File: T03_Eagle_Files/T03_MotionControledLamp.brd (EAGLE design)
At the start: 63.5 x 43.2 mm, 32 parts, among them U1 ATMEGA328P-MU, U4 TPS61161ADRVT, X2 16MHz

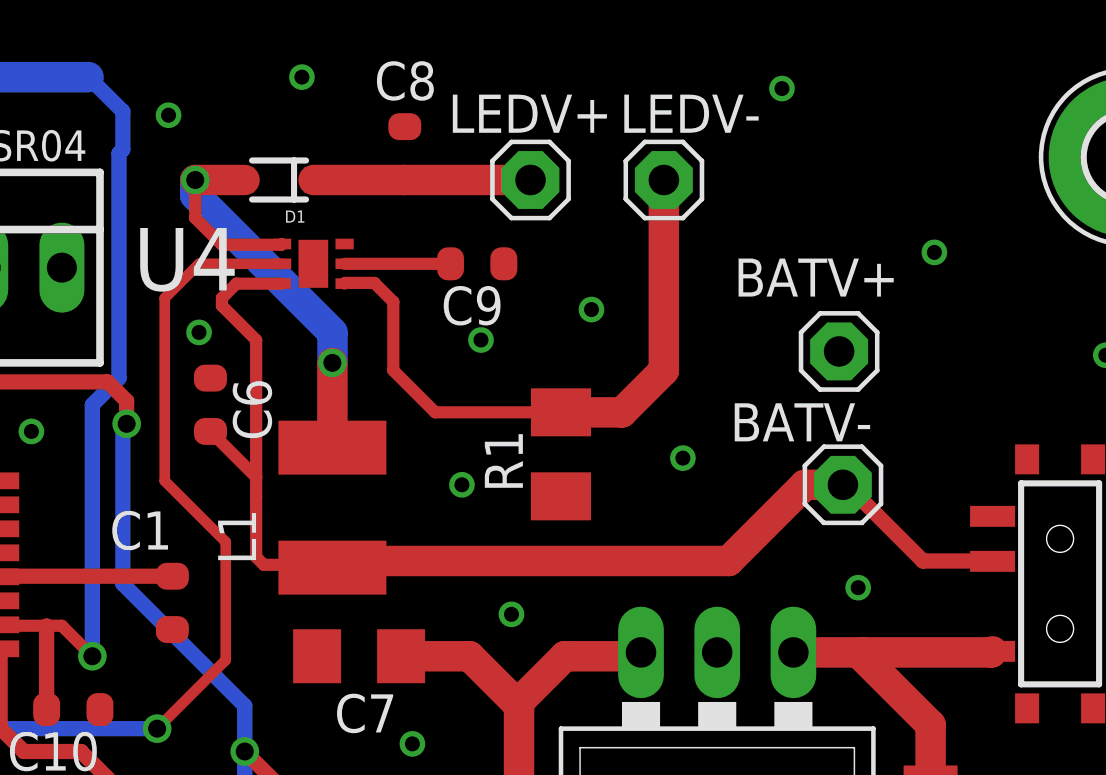
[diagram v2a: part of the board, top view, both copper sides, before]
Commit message: Updated values of components and symbols for Board Layout
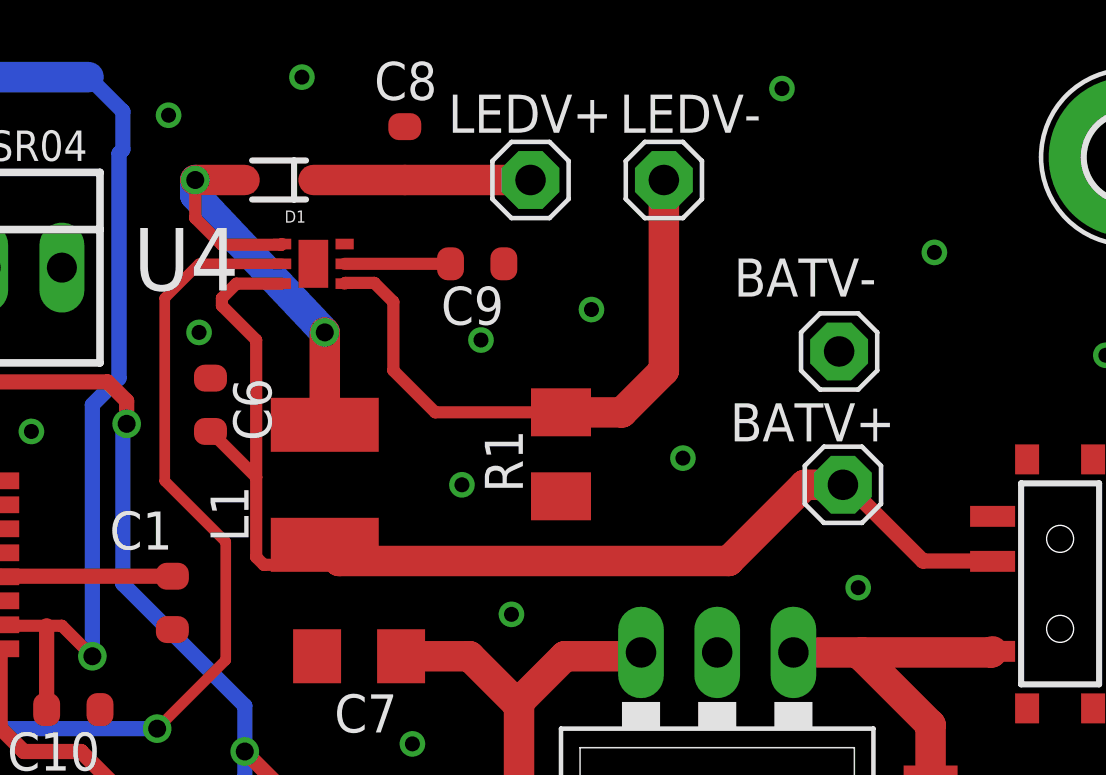
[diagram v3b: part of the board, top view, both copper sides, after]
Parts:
- BATV+: value BAT_GND -> BAT_POS_VOLT
- BATV-: value BAT_POS_VOLT -> BAT_GND
- C8: value 0.1uF -> 10uF
- moved BATV+ 4.45 mm to (48.9, 26.8)
- moved BATV- 4.45 mm to (48.8, 31.2)
- moved L1 0.80 mm to (31.6, 26.8)
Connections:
- net +V_BAT: now also BATV+.1; no longer BATV-.1
- net GND: now also BATV-.1; no longer BATV+.1
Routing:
- net SW: track 17.0 -> 16.1 mm
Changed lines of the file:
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@@
 <element name="C6" library="Smartprj" package="C0603-ROUND" value="1uF" x="27.813" y="29.464" rot="R270"/>
 <element name="C7" library="rcl" package="C1206" value="10uF" x="32.766" y="21.082" rot="R180"/>
-<element name="C8" library="Smartprj" package="C0603-ROUND" value="0.1uF" x="34.29" y="37.846" smashed="yes" rot="R270">
+<element name="C8" library="Smartprj" package="C0603-ROUND" value="10uF" x="34.29" y="37.846" smashed="yes" rot="R270">
 <attribute name="NAME" x="33.274" y="39.624" size="1.27" layer="25"/>
 <attribute name="VALUE" x="32.258" y="38.735" size="1.27" layer="27" rot="R270"/>
@@
 <element name="L7805" library="v-reg" package="78XXL" value="L7805" x="44.704" y="17.399" rot="R180"/>
 <element name="JP1" library="SparkFun-Connectors" package="2X5-SHROUDED_LOCK" value="AVR_SPI_PROG" x="16.51" y="12.446" rot="R90"/>
-<element name="BATV-" library="adafruit" package="1X01" value="BAT_POS_VOLT" x="48.895" y="26.797" smashed="yes">
+<element name="BATV+" library="adafruit" package="1X01" value="BAT_POS_VOLT" x="48.895" y="26.797" smashed="yes">
 <attribute name="NAME" x="45.1358" y="28.2448" size="1.27" layer="25" ratio="10"/>
 <attribute name="VALUE" x="47.625" y="23.622" size="1.27" layer="27"/>
 </element>
-<element name="BATV+" library="adafruit" package="1X01" value="BAT_GND" x="48.768" y="31.242" smashed="yes">
+<element name="BATV-" library="adafruit" package="1X01" value="BAT_GND" x="48.768" y="31.242" smashed="yes">
 <attribute name="NAME" x="45.2628" y="33.0708" size="1.27" layer="25" ratio="10"/>
 <attribute name="VALUE" x="48.514" y="33.274" size="1.27" layer="27"/>
 </element>
-<element name="L1" library="rcl" package="L4532P" value="22uH" x="31.877" y="26.035" smashed="yes" rot="R90">
-<attribute name="NAME" x="29.337" y="24.13" size="1.27" layer="25" rot="R90"/>
-<attribute name="VALUE" x="35.687" y="24.13" size="1.27" layer="27" rot="R90"/>
+<element name="L1" library="rcl" package="L4532P" value="22uH" x="31.623" y="26.797" smashed="yes" rot="R90">
+<attribute name="NAME" x="29.083" y="24.892" size="1.27" layer="25" rot="R90"/>
+<attribute name="VALUE" x="35.433" y="24.892" size="1.27" layer="27" rot="R90"/>
 </element>
 <element name="PWR_SWTCH" library="SparkFun-Electromechanical" package="KPS-1290" value="SWITCH_SPDT" x="56.134" y="23.495" rot="R90">
@@
 <contactref element="C7" pad="2"/>
 <contactref element="C5" pad="2"/>
-<contactref element="BATV+" pad="1"/>
+<contactref element="BATV-" pad="1"/>
 <contactref element="L7805" pad="GND"/>
 <contactref element="JP1" pad="6"/>
@@
 <contactref element="L1" pad="2"/>
 <contactref element="D1" pad="A"/>
-<wire x1="31.877" y1="28.035" x2="31.877" y2="30.861" width="1.016" layer="1"/>
-<via x="31.877" y="30.861" extent="1-16" drill="0.6"/>
+<wire x1="31.623" y1="28.797" x2="31.623" y2="31.877" width="1.016" layer="1"/>
+<via x="31.623" y="31.877" extent="1-16" drill="0.6"/>
 <via x="27.305" y="36.957" extent="1-16" drill="0.6"/>
 <wire x1="27.305" y1="36.957" x2="28.949" y2="36.957" width="1.016" layer="1"/>
-<wire x1="31.877" y1="30.861" x2="31.877" y2="31.877" width="1.016" layer="16"/>
-<wire x1="31.877" y1="31.877" x2="27.305" y2="36.449" width="1.016" layer="16"/>
+<wire x1="31.623" y1="31.877" x2="27.305" y2="36.449" width="1.016" layer="16"/>
 <wire x1="27.305" y1="36.449" x2="27.305" y2="36.957" width="1.016" layer="16"/>
 <wire x1="30.2006" y1="34.8234" x2="30.1752" y2="34.798" width="0.4064" layer="1"/>
@@
 <signal name="+V_BAT">
 <contactref element="PWR_SWTCH" pad="P"/>
-<contactref element="BATV-" pad="1"/>
+<contactref element="BATV+" pad="1"/>
 <contactref element="C6" pad="2"/>
 <contactref element="U4" pad="6"/>
 <contactref element="L1" pad="1"/>
-<wire x1="31.877" y1="24.035" x2="32.099" y2="24.257" width="1.016" layer="1"/>
+<wire x1="31.623" y1="24.797" x2="32.099" y2="24.257" width="1.016" layer="1"/>
 <wire x1="32.099" y1="24.257" x2="45.085" y2="24.257" width="1.016" layer="1"/>
 <wire x1="45.085" y1="24.257" x2="47.625" y2="26.797" width="1.016" layer="1"/>
@@
 <wire x1="31.972" y1="24.13" x2="29.591" y2="24.13" width="0.4064" layer="1"/>
 <wire x1="29.591" y1="24.13" x2="29.337" y2="24.384" width="0.4064" layer="1"/>
-<wire x1="29.337" y1="24.384" x2="29.337" y2="26.416" width="0.4064" layer="1"/>
+<wire x1="29.337" y1="24.384" x2="29.337" y2="27.051" width="0.4064" layer="1"/>
 <wire x1="29.337" y1="27.051" x2="29.337" y2="31.623" width="0.4064" layer="1"/>
 <wire x1="29.337" y1="31.623" x2="28.194" y2="32.766" width="0.4064" layer="1"/>
@@
 <wire x1="28.6766" y1="33.5026" x2="30.2006" y2="33.5026" width="0.4064" layer="1"/>
 <wire x1="27.813" y1="28.575" x2="29.337" y2="27.051" width="0.4064" layer="1"/>
-<wire x1="29.337" y1="27.051" x2="29.337" y2="26.416" width="0.4064" layer="1"/>
 </signal>
 <signal name="TRIG">

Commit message: Added molex headers to schematic
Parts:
- removed BATV+: BAT_POS_VOLT, adafruit:1X01
- removed BATV-: BAT_GND, adafruit:1X01
- removed LEDV+: LED_V+, adafruit:1X01
- removed LEDV-: LED_V-, adafruit:1X01
- removed PWR_SWTCH: SWITCH_SPDT, SparkFun-Electromechanical:KPS-1290
- added 12V, LED_OUT, PWR_SW: 22-23-2021, con-molex:22-23-2021
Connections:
- net +V_BAT: now also 12V.2, PWR_SW.1; no longer BATV+.1, PWR_SWTCH.P
- net FB: now also LED_OUT.2; no longer LEDV-.1
- net GND: now also 12V.1; no longer BATV-.1
- net LED_V+: now also LED_OUT.1; no longer LEDV+.1
- net N$4: now also PWR_SW.2; no longer PWR_SWTCH.O
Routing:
- net +V_BAT: track 41.0 -> 33.7 mm
- net FB: track 20.7 -> 14.4 mm
- net LED_V+: track 7.23 -> 3.04 mm
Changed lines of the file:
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@@
 <element name="L7805" library="v-reg" package="78XXL" value="L7805" x="44.704" y="17.399" rot="R180"/>
 <element name="JP1" library="SparkFun-Connectors" package="2X5-SHROUDED_LOCK" value="AVR_SPI_PROG" x="16.51" y="12.446" rot="R90"/>
-<element name="BATV+" library="adafruit" package="1X01" value="BAT_POS_VOLT" x="48.895" y="26.797" smashed="yes">
-<attribute name="NAME" x="45.1358" y="28.2448" size="1.27" layer="25" ratio="10"/>
-<attribute name="VALUE" x="47.625" y="23.622" size="1.27" layer="27"/>
-</element>
-<element name="BATV-" library="adafruit" package="1X01" value="BAT_GND" x="48.768" y="31.242" smashed="yes">
-<attribute name="NAME" x="45.2628" y="33.0708" size="1.27" layer="25" ratio="10"/>
-<attribute name="VALUE" x="48.514" y="33.274" size="1.27" layer="27"/>
-</element>
 <element name="L1" library="rcl" package="L4532P" value="22uH" x="31.623" y="26.797" smashed="yes" rot="R90">
 <attribute name="NAME" x="29.083" y="24.892" size="1.27" layer="25" rot="R90"/>
 <attribute name="VALUE" x="35.433" y="24.892" size="1.27" layer="27" rot="R90"/>
-</element>
-<element name="PWR_SWTCH" library="SparkFun-Electromechanical" package="KPS-1290" value="SWITCH_SPDT" x="56.134" y="23.495" rot="R90">
-<attribute name="PROD_ID" value="SWCH-10651" x="56.134" y="23.495" size="1.778" layer="27" rot="R90" display="off"/>
 </element>
 <element name="R1" library="rcl" package="M1206" value="10" x="39.497" y="27.813" rot="R90"/>
@@
 <attribute name="VALUE" x="13.97" y="28.956" size="1.016" layer="27" ratio="10"/>
 </element>
-<element name="LEDV+" library="adafruit" package="1X01" value="LED_V+" x="38.481" y="36.957" smashed="yes">
-<attribute name="NAME" x="35.7378" y="38.5318" size="1.27" layer="25" ratio="10"/>
-<attribute name="VALUE" x="37.211" y="33.782" size="1.27" layer="27"/>
-</element>
-<element name="LEDV-" library="adafruit" package="1X01" value="LED_V-" x="42.926" y="36.957" smashed="yes">
-<attribute name="NAME" x="41.4528" y="38.5318" size="1.27" layer="25" ratio="10"/>
-<attribute name="VALUE" x="41.656" y="33.782" size="1.27" layer="27"/>
-</element>
 <element name="H1" library="holes" package="2,8-PAD" value="MOUNT-PAD-ROUND2.8" x="4.826" y="4.572"/>
 <element name="H2" library="holes" package="2,8-PAD" value="MOUNT-PAD-ROUND2.8" x="58.166" y="4.826"/>
@@
 </element>
 <element name="C12" library="Smartprj" package="C0603-ROUND" value="0.1uF" x="18.034" y="38.354" rot="MR0"/>
+<element name="PWR_SW" library="con-molex" package="22-23-2021" value="22-23-2021" x="-3.302" y="5.461">
+<attribute name="OC_FARNELL" value="1462926" x="-3.302" y="5.461" size="1.778" layer="27" display="off"/>
+<attribute name="MPN" value="22-23-2021" x="-3.302" y="5.461" size="1.778" layer="27" display="off"/>
+<attribute name="MF" value="MOLEX" x="-3.302" y="5.461" size="1.778" layer="27" display="off"/>
+<attribute name="OC_NEWARK" value="25C3832" x="-3.302" y="5.461" size="1.778" layer="27" display="off"/>
+</element>
+<element name="12V" library="con-molex" package="22-23-2021" value="22-23-2021" x="-9.525" y="5.461">
+<attribute name="OC_FARNELL" value="1462926" x="-9.525" y="5.461" size="1.778" layer="27" display="off"/>
+<attribute name="MPN" value="22-23-2021" x="-9.525" y="5.461" size="1.778" layer="27" display="off"/>
+<attribute name="MF" value="MOLEX" x="-9.525" y="5.461" size="1.778" layer="27" display="off"/>
+<attribute name="OC_NEWARK" value="25C3832" x="-9.525" y="5.461" size="1.778" layer="27" display="off"/>
+</element>
+<element name="LED_OUT" library="con-molex" package="22-23-2021" value="22-23-2021" x="-15.748" y="5.461">
+<attribute name="OC_FARNELL" value="1462926" x="-15.748" y="5.461" size="1.778" layer="27" display="off"/>
+<attribute name="MPN" value="22-23-2021" x="-15.748" y="5.461" size="1.778" layer="27" display="off"/>
+<attribute name="MF" value="MOLEX" x="-15.748" y="5.461" size="1.778" layer="27" display="off"/>
+<attribute name="OC_NEWARK" value="25C3832" x="-15.748" y="5.461" size="1.778" layer="27" display="off"/>
+</element>
 </elements>
 <signals>
@@
 <contactref element="C7" pad="2"/>
 <contactref element="C5" pad="2"/>
-<contactref element="BATV-" pad="1"/>
 <contactref element="L7805" pad="GND"/>
 <contactref element="JP1" pad="6"/>
@@
 <via x="49.403" y="23.368" extent="1-16" drill="0.5"/>
 <via x="44.704" y="13.589" extent="1-16" drill="0.5"/>
+<contactref element="12V" pad="1"/>
+<wire x1="4.699" y1="15.367" x2="-10.795" y2="5.461" width="0" layer="19" extent="1-1"/>
 </signal>
 <signal name="AREF">
@@
 <signal name="N$4">
 <contactref element="C5" pad="1"/>
-<contactref element="PWR_SWTCH" pad="O"/>
 <contactref element="L7805" pad="IN"/>
-<wire x1="53.884" y1="21.245" x2="53.848" y2="21.209" width="1.016" layer="1"/>
 <wire x1="53.848" y1="21.209" x2="49.53" y2="21.209" width="1.016" layer="1"/>
 <wire x1="49.53" y1="21.209" x2="47.244" y2="21.209" width="1.016" layer="1"/>
@@
 <wire x1="51.816" y1="18.796" x2="49.53" y2="21.082" width="1.016" layer="1"/>
 <wire x1="49.53" y1="21.082" x2="49.53" y2="21.209" width="1.016" layer="1"/>
+<contactref element="PWR_SW" pad="2"/>
+<wire x1="-2.032" y1="5.461" x2="47.244" y2="21.209" width="0" layer="19" extent="1-1"/>
 </signal>
 <signal name="RST">
@@
 <contactref element="D1" pad="C"/>
 <contactref element="C8" pad="2"/>
-<contactref element="LEDV+" pad="1"/>
 <wire x1="31.249" y1="36.957" x2="34.29" y2="36.957" width="1.016" layer="1"/>
-<wire x1="34.29" y1="36.957" x2="38.481" y2="36.957" width="1.016" layer="1"/>
+<contactref element="LED_OUT" pad="1"/>
+<wire x1="-17.018" y1="5.461" x2="31.249" y2="36.957" width="0" layer="19" extent="1-1"/>
 </signal>
 <signal name="FB">
 <contactref element="U4" pad="1"/>
 <contactref element="R1" pad="2"/>
-<contactref element="LEDV-" pad="1"/>
 <wire x1="35.303" y1="29.213" x2="39.497" y2="29.213" width="0.4064" layer="1"/>
 <wire x1="32.2834" y1="33.5026" x2="32.3088" y2="33.528" width="0.4064" layer="1"/>
@@
 <wire x1="39.5" y1="29.21" x2="41.529" y2="29.21" width="1.016" layer="1"/>
 <wire x1="41.529" y1="29.21" x2="42.926" y2="30.607" width="1.016" layer="1"/>
-<wire x1="42.926" y1="30.607" x2="42.926" y2="36.957" width="1.016" layer="1"/>
+<contactref element="LED_OUT" pad="2"/>
+<wire x1="-14.478" y1="5.461" x2="32.2834" y2="33.5026" width="0" layer="19" extent="1-1"/>
 </signal>
 <signal name="COMP">
@@
 </signal>
 <signal name="+V_BAT">
-<contactref element="PWR_SWTCH" pad="P"/>
-<contactref element="BATV+" pad="1"/>
 <contactref element="C6" pad="2"/>
 <contactref element="U4" pad="6"/>
@@
 <wire x1="32.099" y1="24.257" x2="45.085" y2="24.257" width="1.016" layer="1"/>
 <wire x1="45.085" y1="24.257" x2="47.625" y2="26.797" width="1.016" layer="1"/>
-<wire x1="47.625" y1="26.797" x2="48.895" y2="26.797" width="1.016" layer="1"/>
-<wire x1="53.884" y1="24.245" x2="53.872" y2="24.257" width="0.508" layer="1"/>
-<wire x1="53.872" y1="24.257" x2="51.562" y2="24.257" width="0.508" layer="1"/>
-<wire x1="51.562" y1="24.257" x2="49.022" y2="26.797" width="0.508" layer="1"/>
-<wire x1="49.022" y1="26.797" x2="48.895" y2="26.797" width="0.508" layer="1"/>
 <wire x1="32.099" y1="24.257" x2="31.972" y2="24.13" width="0.4064" layer="1"/>
 <wire x1="31.972" y1="24.13" x2="29.591" y2="24.13" width="0.4064" layer="1"/>
@@
 <wire x1="28.6766" y1="33.5026" x2="30.2006" y2="33.5026" width="0.4064" layer="1"/>
 <wire x1="27.813" y1="28.575" x2="29.337" y2="27.051" width="0.4064" layer="1"/>
+<contactref element="12V" pad="2"/>
+<contactref element="PWR_SW" pad="1"/>
+<wire x1="-4.572" y1="5.461" x2="29.337" y2="24.384" width="0" layer="19" extent="1-1"/>
+<wire x1="-8.255" y1="5.461" x2="-4.572" y2="5.461" width="0" layer="19" extent="1-1"/>
 </signal>
 <signal name="TRIG">
